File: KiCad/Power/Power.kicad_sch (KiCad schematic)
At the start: 23 parts, among them J2 691137710003, J5 691137710002, J6 691137710002, U1 CD74HC4051E, U11 TL074

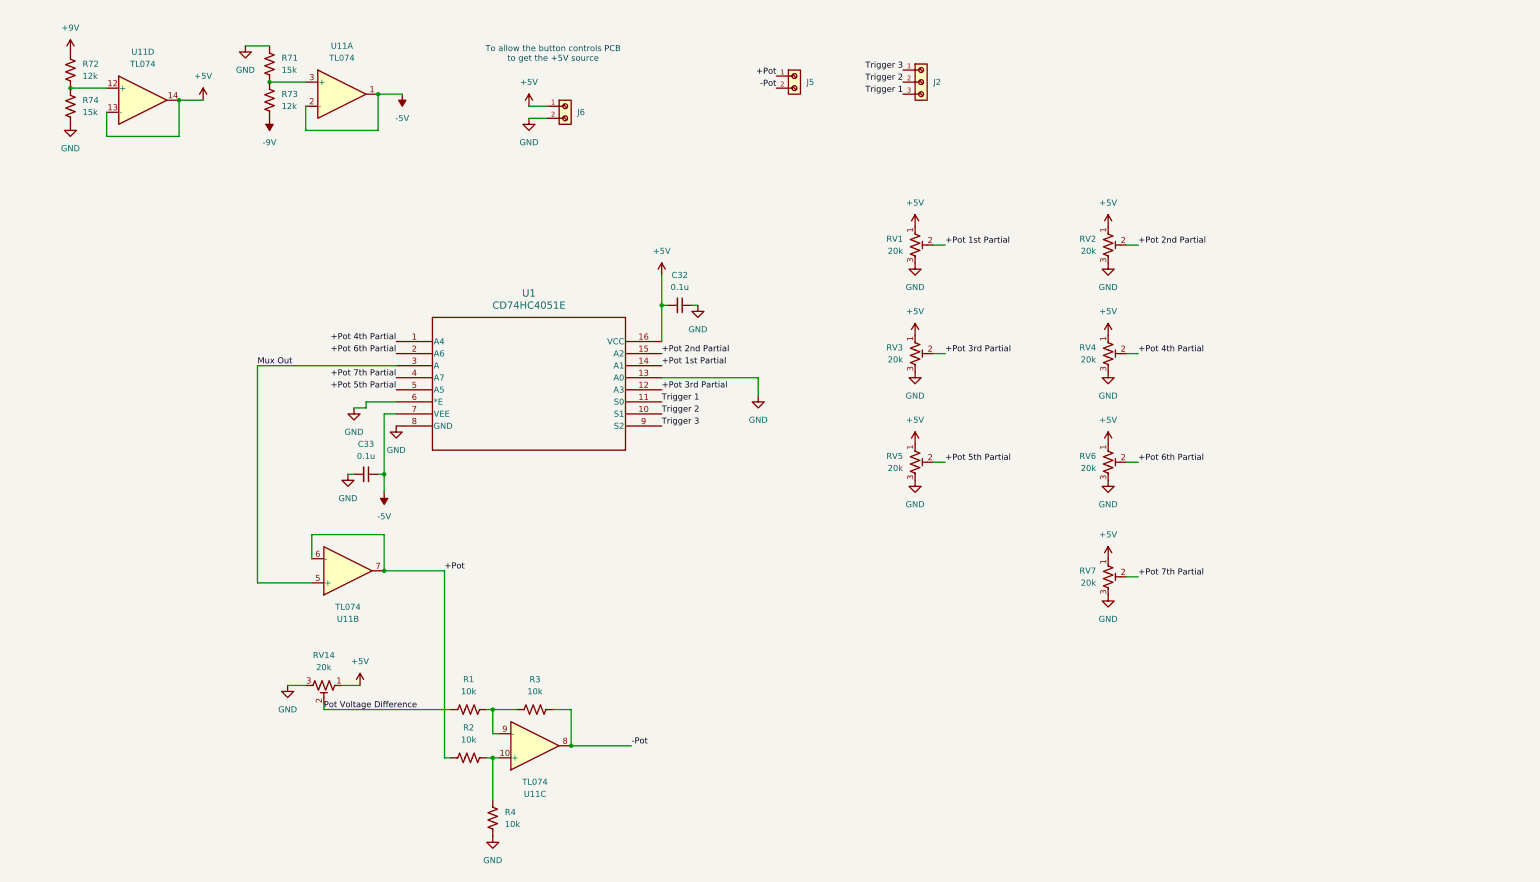
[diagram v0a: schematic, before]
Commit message: started separating into different boards, partially fixed envelope generator
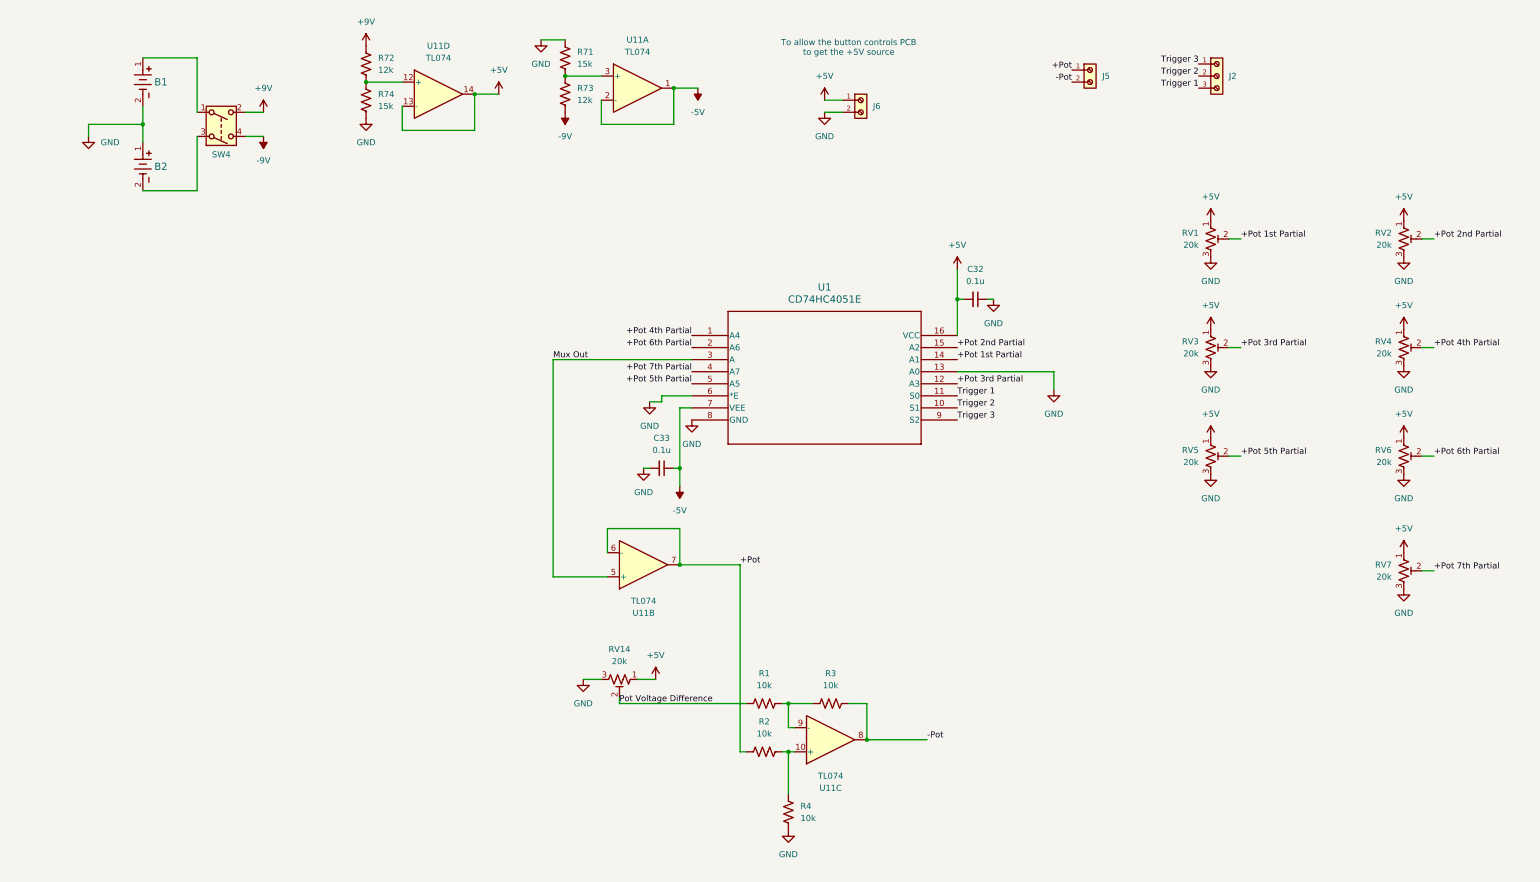
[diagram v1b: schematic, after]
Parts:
- added B1, B2: BC9VPC, Battery Holder BC9VPC:BC9VPC_MPD, symbol 2026-06-10_00-17-41:BC9VPC
- added SW4: SW_DPST, DPST Switch RA83231100:DPST Switch RA83231100, symbol Switch:SW_DPST
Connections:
- net +9V: now also SW4.2
- net -9V: now also SW4.4
- net GND: now also B1.2, B2.1
- new net: B1.1, SW4.1
- new net: B2.2, SW4.3
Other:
- moved on the sheet: C32, C33, J2, J5, J6, R1, R2, R3, R4, R71, R72, R73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

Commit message: fixed power board, replaced sketchy voltage divider - op amp cct. with an LDO to product +5V
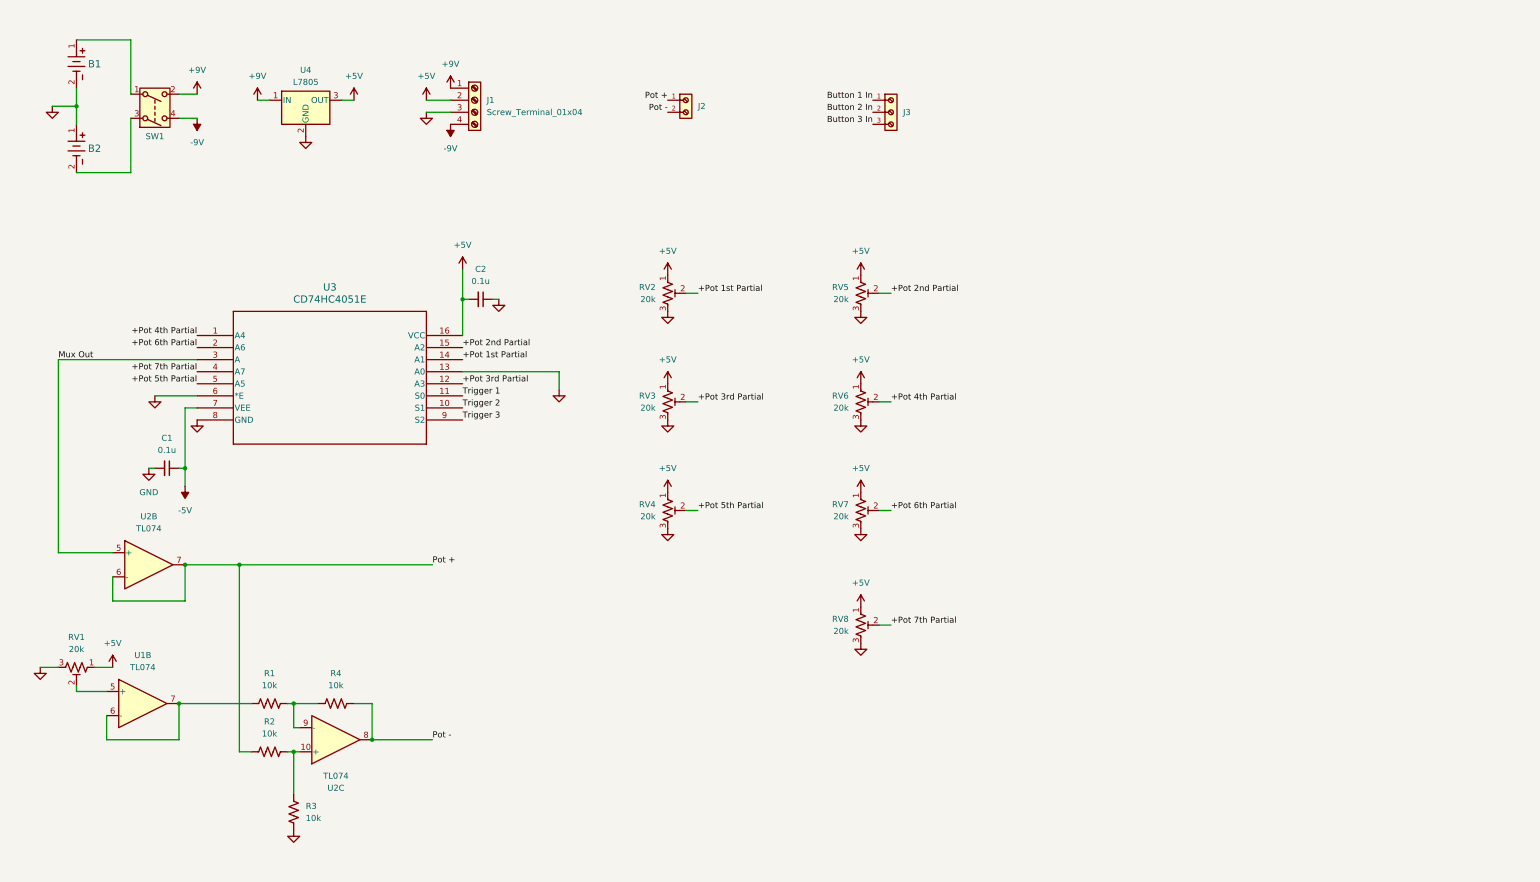
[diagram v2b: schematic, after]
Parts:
- removed J6: 691137710002, Header 691137710002:691137710002, symbol Header 691137710002:691137710002
- removed R71, R74: 15k, Resistor_SMD:R_0603_1608Metric, symbol Device:R_US
- removed R72, R73: 12k, Resistor_SMD:R_0603_1608Metric, symbol Device:R_US
- removed unit 1 of U11
- removed unit 4 of U11
- added J1: Screw_Terminal_01x04, symbol Connector:Screw_Terminal_01x04
- added U1: TL074, Package_DIP:DIP-14_W7.62mm, symbol Amplifier_Operational:TL074
- added U4: L7805, symbol Regulator_Linear:L7805
- renumbered C33 to C1, C32 to C2, J5 to J2, J2 to J3, R4 to R3, R3 to R4, RV14 to RV1, RV1 to RV2, RV5 to RV4, RV2 to RV5, RV4 to RV6, RV6 to RV7, RV7 to RV8, SW4 to SW1, U11 to U2, U1 to U3
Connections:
- net +5V: now also J1.2 (Pin_2), U4.3 (OUT)
- net +9V: now also J1.1 (Pin_1), U4.1 (IN)
- net -9V: now also J1.4 (Pin_4)
- net GND: now also J1.3 (Pin_3), U4.2 (GND)
- net Trigger 1: no longer J3.3
- net Trigger 2: no longer J3.2
- net Trigger 3: no longer J3.1
- net +Pot renamed Pot +
- net -Pot renamed Pot -
- net Pot Voltage Difference: no longer names the net of RV1.2
- net Pot Voltage Difference: now also U1.5 (+); no longer R1.1
- new net: R1.1, U1.6 (-), U1.7
- new net Button 1 In: J3.1
- new net Button 2 In: J3.2
- new net Button 3 In: J3.3
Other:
- note removed: "To allow the button controls PCB to get the +5V source"
- moved on the sheet: B1, B2, C1, C2, J2, J3, R1, R2, R3, R4, RV1, RV2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

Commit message: finished separating into separate kicad projects
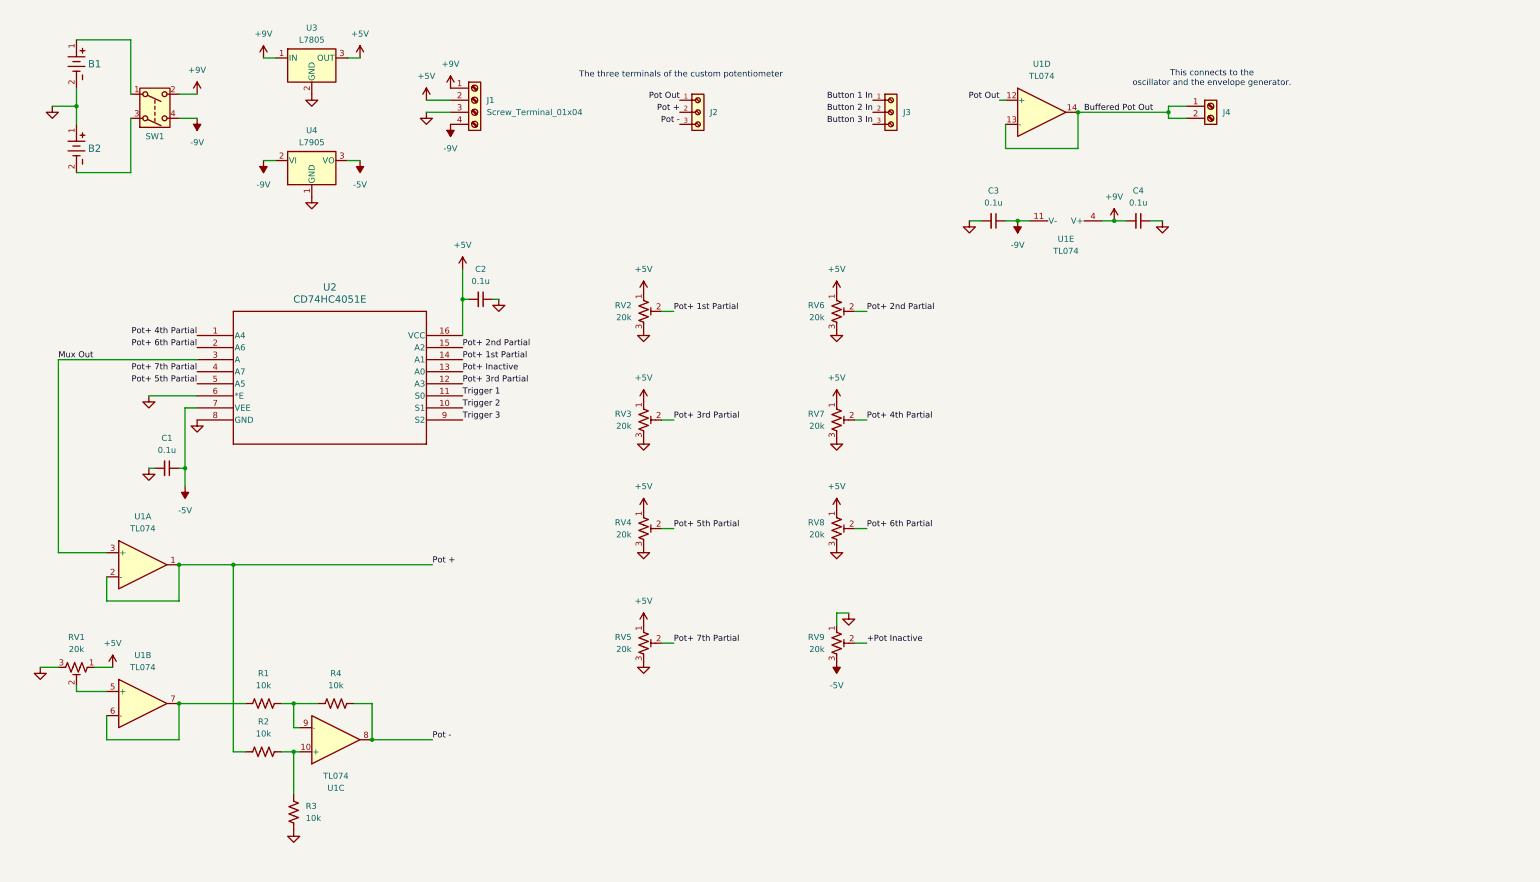
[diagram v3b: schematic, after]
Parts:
- removed J2: 691137710002, Header 691137710002:691137710002, symbol Header 691137710002:691137710002
- added C3, C4: 0.1u, symbol Device:C_Small
- added J2: 691137710003, Header 691137710003:691137710003, symbol Header 691137710003:691137710003
- added J4: Screw_Terminal_01x02, symbol Connector:Screw_Terminal_01x02
- added RV9: 20k, Potentiometer_SMD:Potentiometer_Bourns_TC33X_Vertical, symbol Device:R_Potentiometer_Trim_US
- added unit 5 of U1
- added unit 4 of U1
- added U4: L7905, symbol Regulator_Linear:L7905
- renumbered RV8 to RV5, RV5 to RV6, RV6 to RV7, RV7 to RV8, U2 to U1, U3 to U2, U4 to U3
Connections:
- net +9V: now also C4.2, U1.4 (V+)
- net -5V: now also RV9.3, U4.3 (VO)
- net -9V: now also C3.1, U1.11 (V-), U4.2 (VI)
- net GND: now also C3.2, C4.1, RV9.1, U4.1 (GND); no longer U2.13 (A0)
- net Mux Out: now also U1.3 (+); no longer U1.5 (+)
- net Pot +: now also U1.1, U1.2 (-), J2.2; no longer U1.6 (-), U1.7
- net Pot -: now also J2.3
- net +Pot 1st Partial renamed Pot+ 1st Partial
- net +Pot 2nd Partial renamed Pot+ 2nd Partial
- net +Pot 3rd Partial renamed Pot+ 3rd Partial
- net +Pot 4th Partial renamed Pot+ 4th Partial
- net +Pot 5th Partial renamed Pot+ 5th Partial
- net +Pot 6th Partial renamed Pot+ 6th Partial
- net +Pot 7th Partial renamed Pot+ 7th Partial
- new net +Pot Inactive: RV9.2
- new net Buffered Pot Out: J4.1 (Pin_1), J4.2 (Pin_2), U1.13 (-), U1.14
- new net Pot Out: J2.1, U1.12 (+)
- new net Pot+ Inactive: U2.13 (A0)
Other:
- note added: "The three terminals of the custom potentiometer"
- note added: "This connects to the oscillator and the envelope generator."
- moved on the sheet: R1, R2, RV2, RV3, RV4, RV5, RV6, RV7, RV8, U1A, U3

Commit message: added test points
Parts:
- added TP? (x18): TestPoint_Small, symbol Connector:TestPoint_Small
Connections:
- net +Pot Inactive: now also TP?.1
- net Buffered Pot Out: now also TP?.1
- net Button 1 In: now also TP?.1
- net Button 2 In: now also TP?.1
- net Button 3 In: now also TP?.1
- net GND: now also TP?.1
- net Mux Out: now also TP?.1
- net Pot +: now also TP?.1
- net Pot -: now also TP?.1
- net Pot Out: now also TP?.1
- net Pot+ 1st Partial: now also TP?.1
- net Pot+ 2nd Partial: now also TP?.1
- net Pot+ 3rd Partial: now also TP?.1
- net Pot+ 4th Partial: now also TP?.1
- net Pot+ 5th Partial: now also TP?.1
- net Pot+ 6th Partial: now also TP?.1
- net Pot+ 7th Partial: now also TP?.1
- net Pot Voltage Difference: now reaches RV1.2, U1.5 (+)
- net Pot Voltage Difference: now also TP?.1
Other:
- moved on the sheet: R1, R2, R3, R4, RV1, U1A, U1B, U1C

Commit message: added power indicator LEDs
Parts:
- added D1, D2, D3, D4: LED, symbol Device:LED
- added R5, R6, R7, R8: R_US, symbol Device:R_US
- gave numbers to parts that had none: 18
- renumbered U2 to U1, U1 to U2
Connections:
- net +5V: now also D2.2 (A)
- net +9V: now also D1.2 (A)
- net -5V: now also R7.2
- net -9V: now also R8.2
- net GND: now also D3.2 (A), D4.2 (A), R5.2, R6.2
- new net: D1.1 (K), R5.1
- new net: D3.1 (K), R7.1
- new net: D2.1 (K), R6.1
- new net: D4.1 (K), R8.1
